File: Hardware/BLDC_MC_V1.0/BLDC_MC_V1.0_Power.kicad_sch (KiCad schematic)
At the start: 44 parts, among them J1 Conn_01x03_Pin, J2 Conn_01x03_Pin, U1 LM76005RNPR, U5 LDL1117S33R, U7 NCV4274ADT50RKG

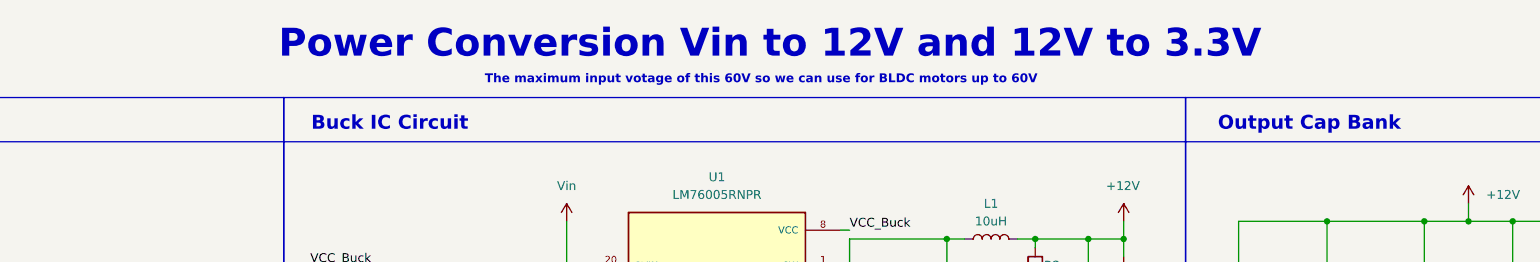
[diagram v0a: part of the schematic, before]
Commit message: Adjust the connections between sheets
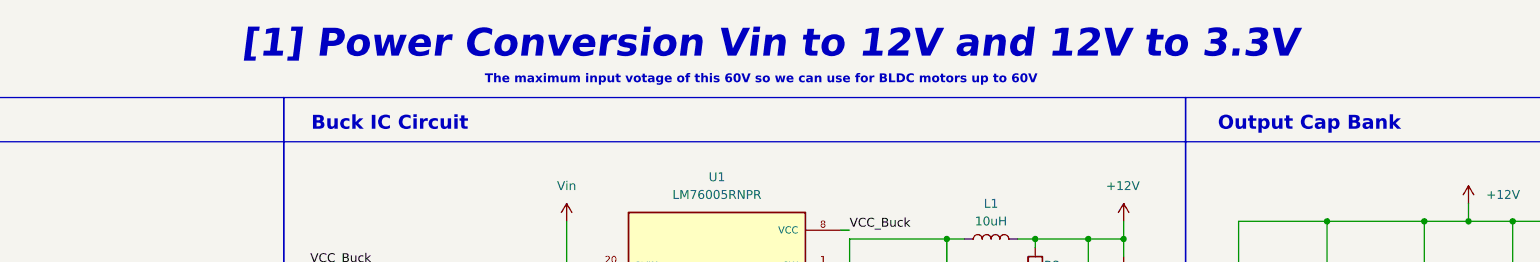
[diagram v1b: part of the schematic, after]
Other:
- note added: "[1] Power Conversion Vin to 12V and 12V to 3.3V"
- note removed: "Power Conversion Vin to 12V and 12V to 3.3V"
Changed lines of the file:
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@@
 		)
 	)
-	(text "Power Conversion Vin to 12V and 12V to 3.3V"
+	(text "[1] Power Conversion Vin to 12V and 12V to 3.3V"
 		(exclude_from_sim no)
 		(at 143.51 19.05 0)
@@
 				(thickness 0.8)
 				(bold yes)
+				(italic yes)
 				(color 132 0 0 1)
 			)

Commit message: Solve all errors and wornings in project
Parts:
- added C89, C90: 100nF, Capacitor_SMD:C_0805_2012Metric, symbol Device:C
- added CR10: SMDJ110CA, BLDC_Motor_Driver_Components_Footprint:SMDJSeries_LTF, symbol SMDJ110CA:SMDJ110CA
- added NT4, NT5: NetTie_2, NetTie:NetTie-2_SMD_Pad2.0mm, symbol Device:NetTie_2
- added Q7: BSC027N10NS5ATMA1, BLDC_Motor_Driver_Components_Footprint:PG-TSON-8-3_INF, symbol BSC027N10NS5ATMA1:BSC027N10NS5ATMA1
- added TP1, TP2, TP3, TP4: TestPoint, Connector_Pin:Pin_D0.9mm_L10.0mm_W2.4mm_FlatFork, symbol Connector:TestPoint
- added U16: LM74700QDRQ1, BLDC_Motor_Driver_Components_Footprint:SOIC8_D_TEX, symbol LM74700QDRQ1:LM74700QDRQ1
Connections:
- net +12V: now also TP1.1
- net +3.3V: now also TP3.1
- net +5V: now also TP2.1
- net AGND: now also NT4.2; no longer C10.2, C26.1, C27.1, C29.2, C3.2, C30.2, C31.2, C33.2, C34.2, C35.2, C36.2, C37.2, C4.2, C5.1, C53.2, C54.2, C55.2, C56.2, C6.1, C7.2, C8.2, C9.2, D1.1 (K), D2.1 (K), D3.1 (K), D4.1 (K), R1.2, R3.2, R4.2, U1.19 (NC), U1.24 (PGND), U1.25 (PGND), U1.26 (PGND), U1.27 (NC), U1.28 (NC), U1.29 (NC), U1.30 (NC), U1.31 (EP), U5.1 (GND), U7.2 (GND)
- net Vin: now also Q7.1, Q7.2, Q7.3, TP4.1, U16.8 (CATHODE)
- new net: U16.3 (N.C), U16.7 (N.C)
- new net: C89.2, U16.4 (VCAP)
- new net: Q7.4, U16.6 (GATE)
- new net GND: C10.2, C26.1, C27.1, C29.2, C3.2, C30.2, C31.2, C33.2, C34.2, C35.2, C36.2, C37.2, C4.2, C5.1, C53.2, C54.2, C55.2, C56.2, C6.1, C7.2, C8.2, C9.2, D1.1 (K), D2.1 (K), D3.1 (K), D4.1 (K), NT4.1, NT5.1, R1.2, R3.2, R4.2, U1.19 (NC), U1.27 (NC), U1.28 (NC), U1.29 (NC), U1.30 (NC), U1.31 (EP), U5.1 (GND), U7.2 (GND)
- new net GND_In: C90.2, CR10.2, U16.1 (GND)
- new net PGND: NT5.2, U1.24 (PGND), U1.25 (PGND), U1.26 (PGND)
- new net Vin_DC: C89.1, C90.1, CR10.1, Q7.5, Q7.6, Q7.7, Q7.8, U16.2 (EN), U16.5 (ANODE)
- no-connect marks 0 -> 1
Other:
- note added: "Input PWR Protection"
- moved on the sheet: C31

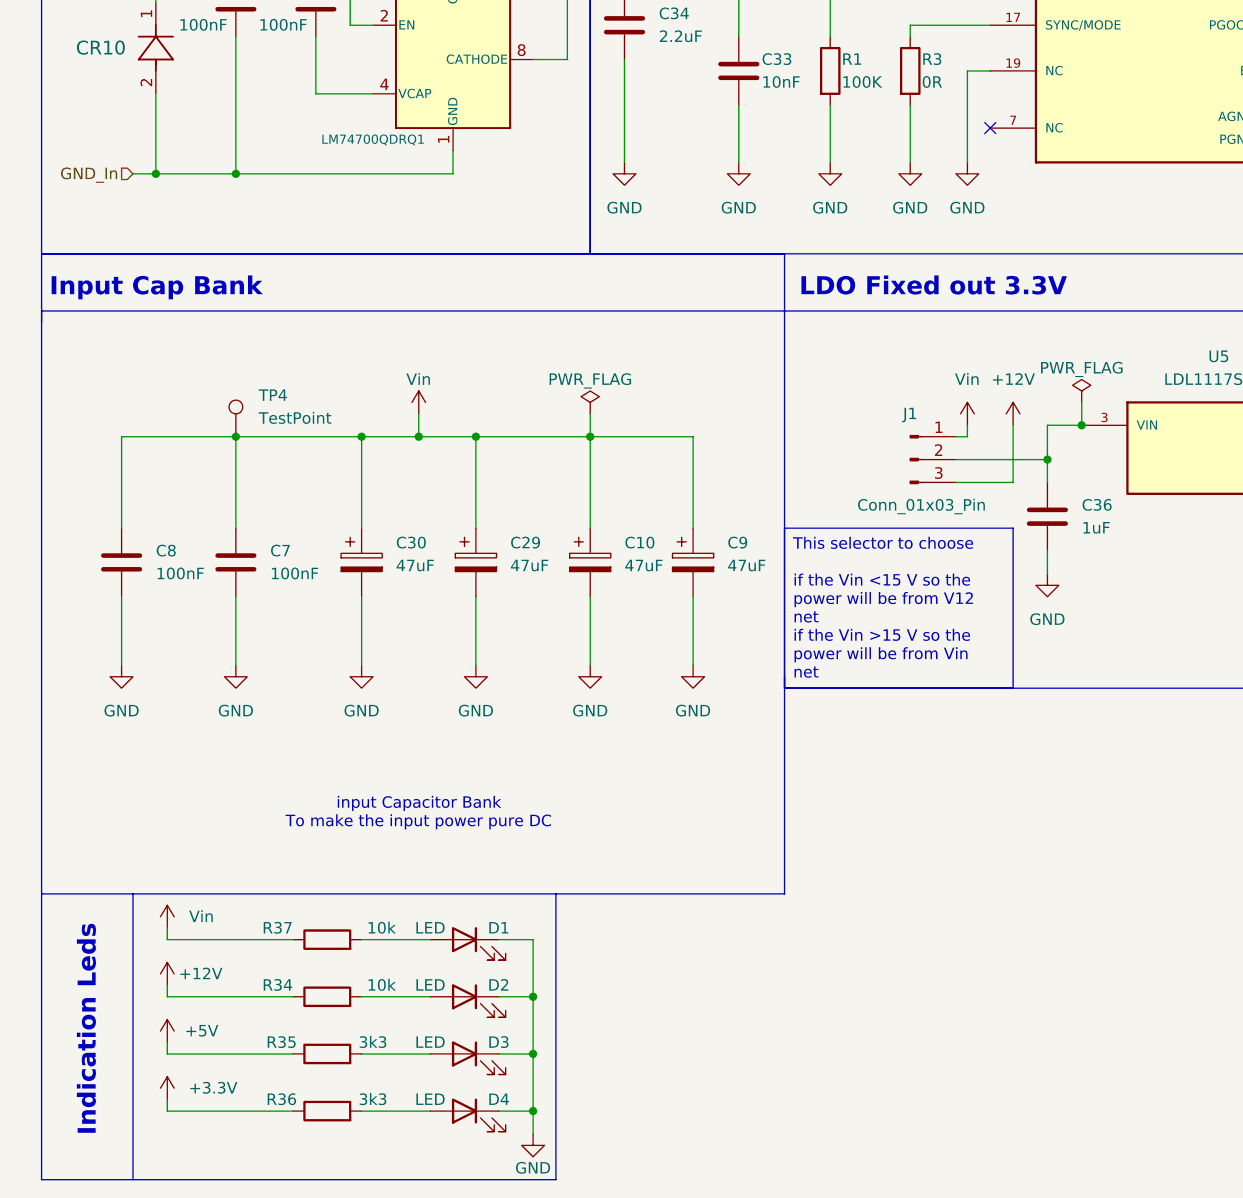
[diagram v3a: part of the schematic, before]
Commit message: Update the component placement of the board
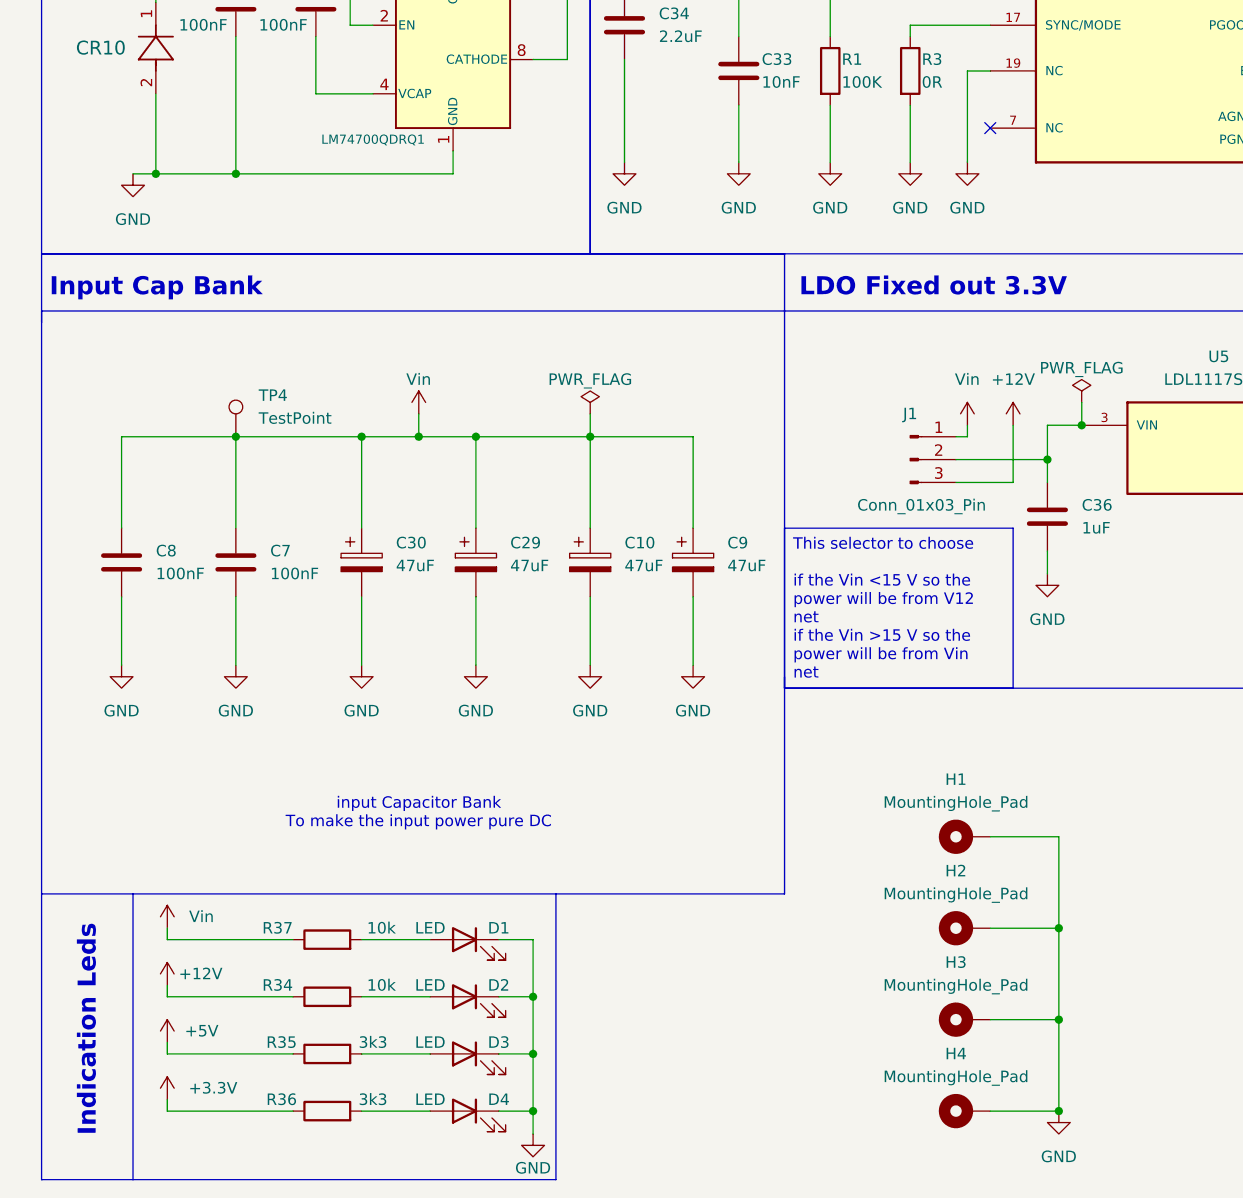
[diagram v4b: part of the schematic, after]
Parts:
- added H1, H2, H3, H4: MountingHole_Pad, MountingHole:MountingHole_2.2mm_M2_Pad_Via, symbol Mechanical:MountingHole_Pad
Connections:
- net GND_In is gone; now on net GND: C90.2, CR10.2, U16.1 (GND)
- net GND: now also H1.1, H2.1, H3.1, H4.1

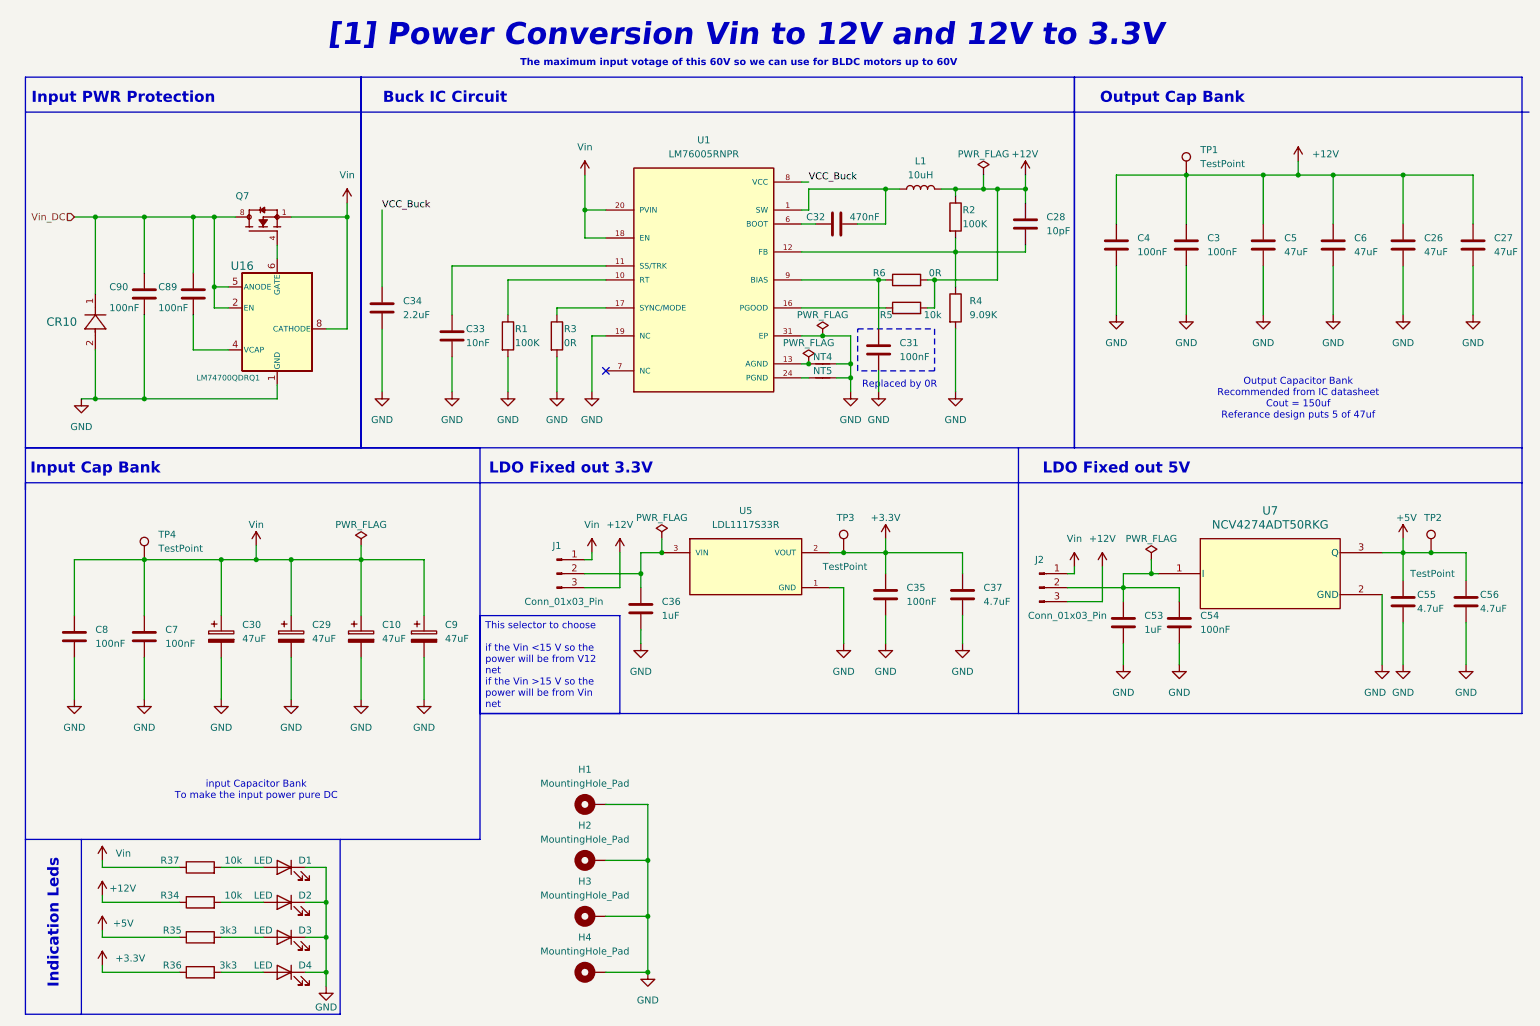
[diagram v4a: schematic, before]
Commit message: Update the components' placement of the board
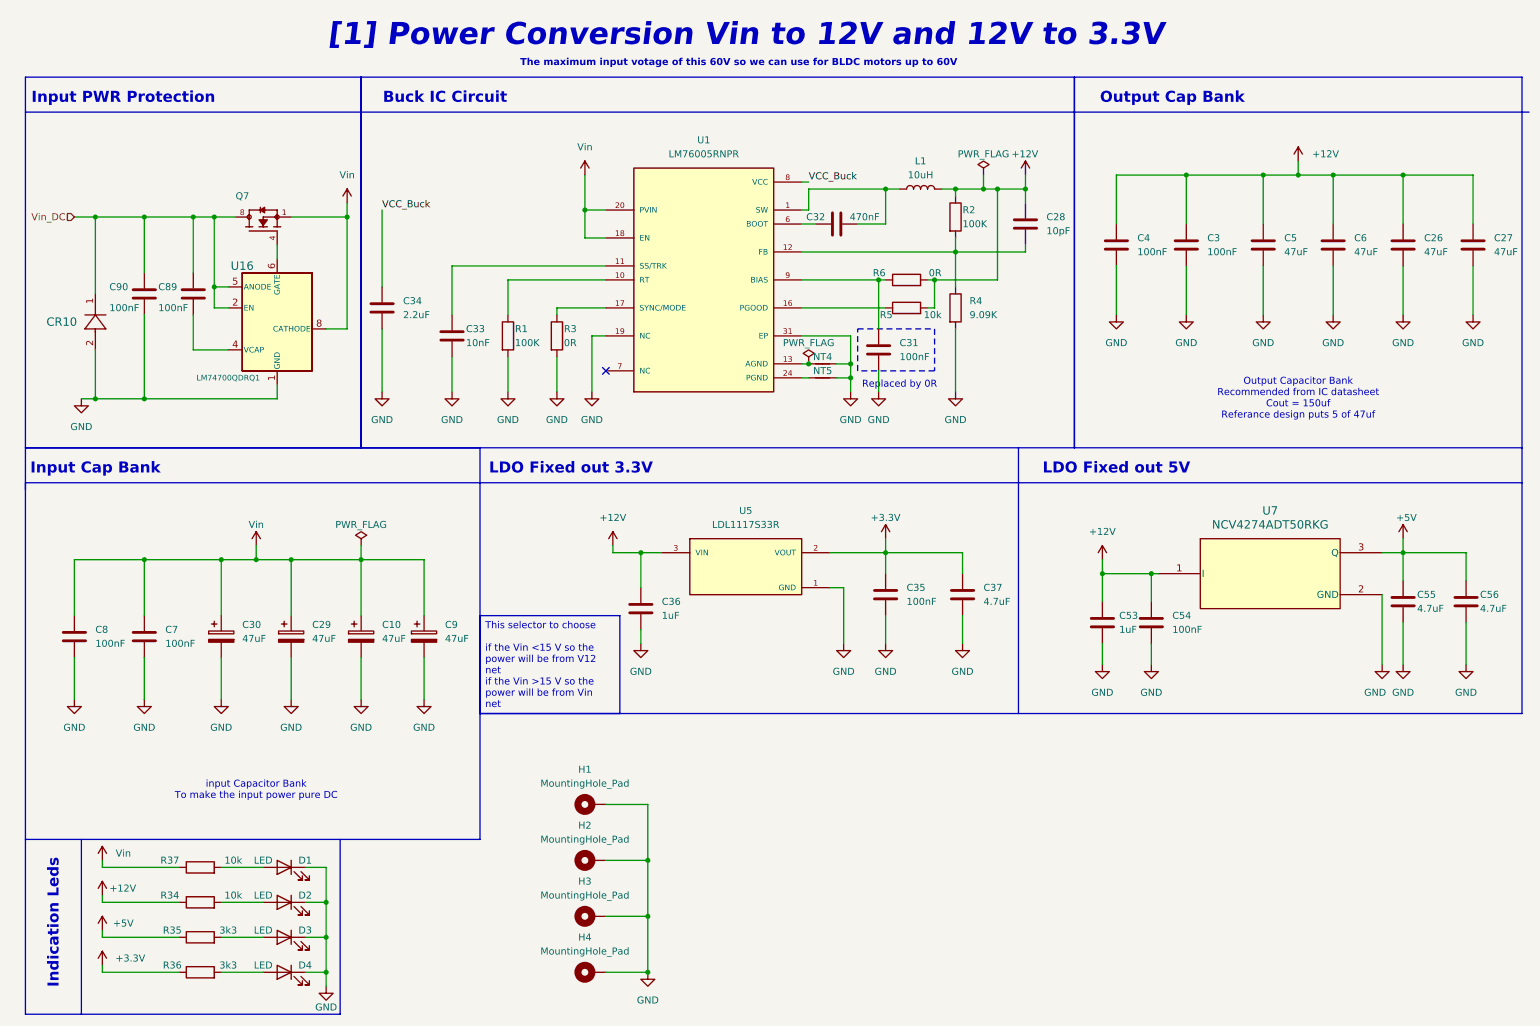
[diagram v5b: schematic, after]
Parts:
- removed J1, J2: Conn_01x03_Pin, Connector_PinHeader_2.54mm:PinHeader_1x03_P2.54mm_Vertical, symbol Connector:Conn_01x03_Pin
- removed TP1, TP2, TP3, TP4: TestPoint, Connector_Pin:Pin_D0.9mm_L10.0mm_W2.4mm_FlatFork, symbol Connector:TestPoint
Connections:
- net +12V: now also C36.1, C53.1, C54.1, U5.3 (VIN), U7.1 (I)
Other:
- moved on the sheet: C53, C54

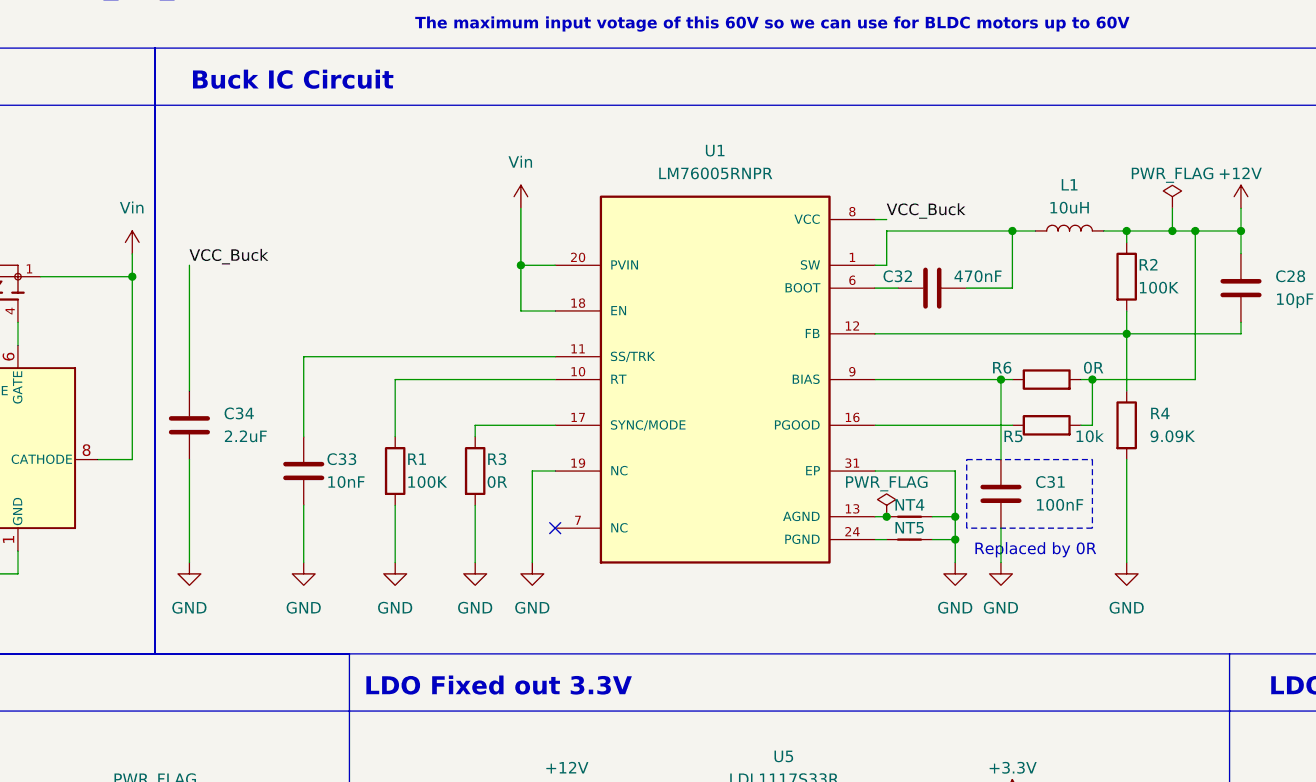
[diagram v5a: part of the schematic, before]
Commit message: Routing Power plans and change the power connedtors
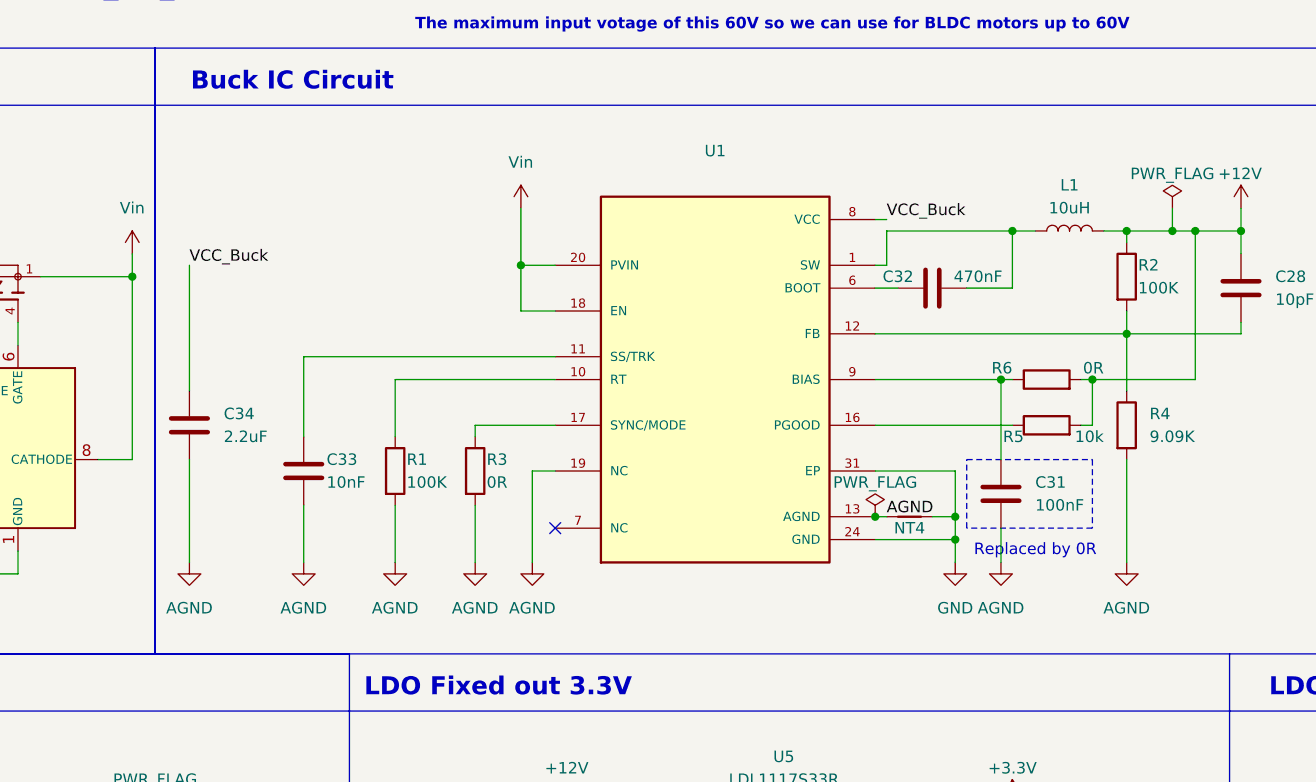
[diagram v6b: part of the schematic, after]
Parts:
- removed NT5: NetTie_2, NetTie:NetTie-2_SMD_Pad2.0mm, symbol Device:NetTie_2
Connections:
- net PGND is gone; now on net GND: U1.24 (GND), U1.25 (GND), U1.26 (GND)
- net AGND: now also C31.2, C33.2, C34.2, R1.2, R3.2, R4.2, U1.19 (NC), U1.27 (NC), U1.28 (NC), U1.29 (NC), U1.30 (NC)
- net GND: no longer C31.2, C33.2, C34.2, R1.2, R3.2, R4.2, U1.19 (NC), U1.27 (NC), U1.28 (NC), U1.29 (NC), U1.30 (NC)
